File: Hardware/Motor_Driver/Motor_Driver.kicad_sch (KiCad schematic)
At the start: 2 parts, among them U1 IR4301, U2 LM4766

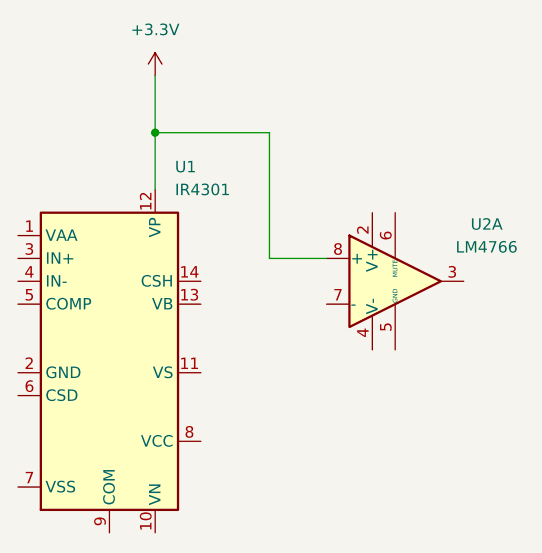
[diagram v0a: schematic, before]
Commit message: endret på shcemtatic, fjernet opamp
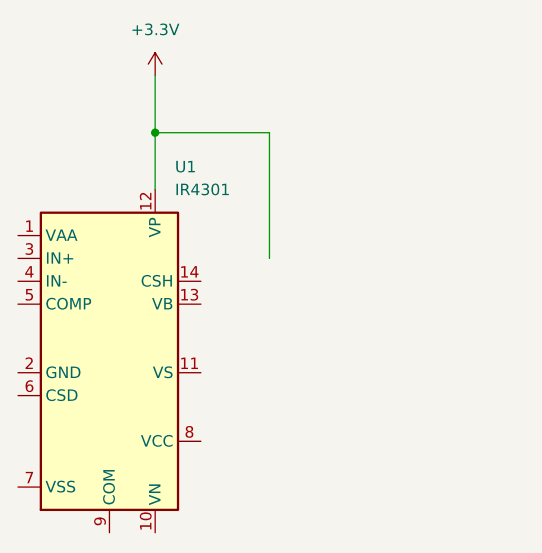
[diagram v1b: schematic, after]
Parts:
- removed U2: LM4766, Package_TO_SOT_THT:TO-220-15_P2.54x2.54mm_StaggerOdd_Lead4.58mm_Vertical, symbol Amplifier_Audio:LM4766
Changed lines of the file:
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@@
-		)
-	)
-	(wire
-		(pts
-			(xy 154.94 73.66) (xy 148.59 73.66)
-		)
-		(stroke
-			(width 0)
-			(type default)
-		)
-	)
-	(symbol
-		(lib_id "Amplifier_Audio:LM4766")
-		(at 162.56 76.2 0)
-		(unit 1)
-		(exclude_from_sim no)
-		(in_bom yes)
-		(on_board yes)
-		(dnp no)
-		(fields_autoplaced yes)
-		(property "Reference" "U2"
-			(at 172.72 69.8814 0)
-			(effects
-				(font
-					(size 1.27 1.27)
-				)
-			)
-		)
-		(property "Value" "LM4766"
-			(at 172.72 72.4214 0)
-			(effects
-				(font
-					(size 1.27 1.27)
-				)
-			)
-		)
-		(property "Footprint" "Package_TO_SOT_THT:TO-220-15_P2.54x2.54mm_StaggerOdd_Lead4.58mm_Vertical"
-			(at 162.56 76.2 0)
-			(effects
-				(font
-					(size 1.27 1.27)
-					(italic yes)
-				)
-				(hide yes)
-			)
-		)
-		(property "Datasheet" "http://www.ti.com/lit/ds/symlink/lm4766.pdf"
-			(at 162.56 76.2 0)
-			(effects
-				(font
-					(size 1.27 1.27)
-				)
-				(hide yes)
-			)
-		)
-		(property "Description" "Overture Audio Power Amplifier Series Dual 40W Audio Power Amplifier with Mute, TO-220-15"
-			(at 162.56 76.2 0)
-			(effects
-				(font
-					(size 1.27 1.27)
-				)
-				(hide yes)
-			)
-		)
-		(pin "3"
-		)
-		(pin "13"
-		)
-		(pin "15"
-		)
-		(pin "2"
-		)
-		(pin "5"
-		)
-		(pin "11"
-		)
-		(pin "9"
-		)
-		(pin "1"
-		)
-		(pin "14"
-		)
-		(pin "10"
-		)
-		(pin "6"
-		)
-		(pin "7"
-		)
-		(pin "4"
-		)
-		(pin "8"
-		)
-		(pin "12"
-		)
-		(instances
-			(project ""
-				(path "/ef03e5fb-dcf6-48d2-925e-8f1f54ddcbda"
-					(reference "U2")
-					(unit 1)
-				)
-			)
 		)
 	)
@@
 		)
 		(instances
-			(project ""
+			(project "Motor_Driver"
 				(path "/ef03e5fb-dcf6-48d2-925e-8f1f54ddcbda"
 					(reference "#PWR01")
@@
 		)
 		(instances
-			(project ""
+			(project "Motor_Driver"
 				(path "/ef03e5fb-dcf6-48d2-925e-8f1f54ddcbda"
 					(reference "U1")

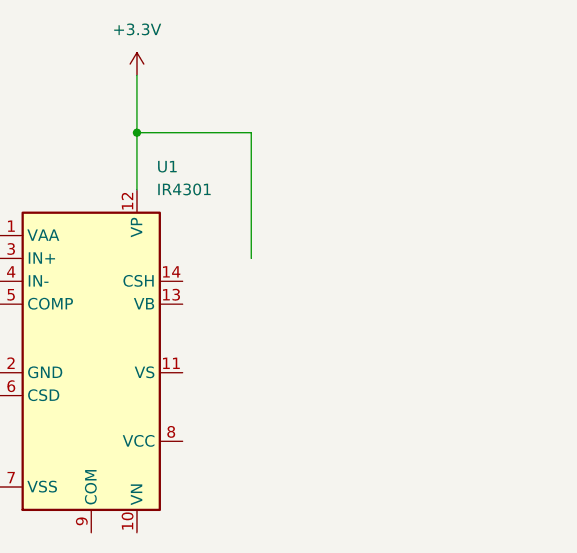
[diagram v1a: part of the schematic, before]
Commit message: La til en AND gate
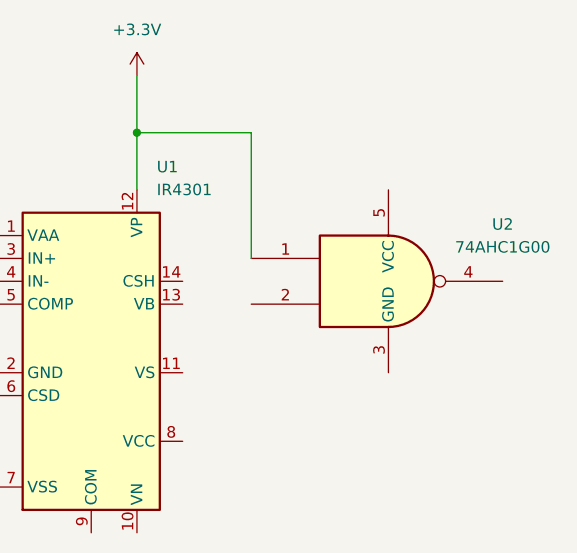
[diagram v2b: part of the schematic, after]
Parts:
- added U2: 74AHC1G00, symbol 74xGxx:74AHC1G00
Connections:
- net +3.3V: now also U2.1
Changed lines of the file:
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@@
+	)
+	(symbol
+		(lib_id "74xGxx:74AHC1G00")
+		(at 163.83 76.2 0)
+		(unit 1)
+		(exclude_from_sim no)
+		(in_bom yes)
+		(on_board yes)
+		(dnp no)
+		(fields_autoplaced yes)
+		(property "Reference" "U2"
+			(at 176.53 69.8814 0)
+			(effects
+				(font
+					(size 1.27 1.27)
+				)
+			)
+		)
+		(property "Value" "74AHC1G00"
+			(at 176.53 72.4214 0)
+			(effects
+				(font
+					(size 1.27 1.27)
+				)
+			)
+		)
+		(property "Footprint" ""
+			(at 163.83 76.2 0)
+			(effects
+				(font
+					(size 1.27 1.27)
+				)
+				(hide yes)
+			)
+		)
+		(property "Datasheet" "http://www.ti.com/lit/sg/scyt129e/scyt129e.pdf"
+			(at 163.83 76.2 0)
+			(effects
+				(font
+					(size 1.27 1.27)
+				)
+				(hide yes)
+			)
+		)
+		(property "Description" "Single NAND Gate, Low-Voltage CMOS"
+			(at 163.83 76.2 0)
+			(effects
+				(font
+					(size 1.27 1.27)
+				)
+				(hide yes)
+			)
+		)
+		(pin "4"
+		)
+		(pin "5"
+		)
+		(pin "2"
+		)
+		(pin "3"
+		)
+		(pin "1"
+		)
+		(instances
+			(project ""
+				(path "/ef03e5fb-dcf6-48d2-925e-8f1f54ddcbda"
+					(reference "U2")
+					(unit 1)
+				)
+			)
+		)
 	)
 	(symbol

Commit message: Lagt inn 2 USB-C porter
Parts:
- removed U1: IR4301, Package_DFN_QFN:Infineon_PQFN-22-15-4EP_6x5mm_P0.65mm, symbol Amplifier_Audio:IR4301
- removed U2: 74AHC1G00, symbol 74xGxx:74AHC1G00
- added P1, P2: USB_C_Plug, symbol Connector:USB_C_Plug
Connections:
- new net: P1.A1 (GND), P1.A12 (GND), P1.B1 (GND), P1.B12 (GND)
- new net: P1.A4 (VBUS), P1.A9 (VBUS), P1.B4 (VBUS), P1.B9 (VBUS)
- new net: P2.A1 (GND), P2.A12 (GND), P2.B1 (GND), P2.B12 (GND)
- new net: P2.A4 (VBUS), P2.A9 (VBUS), P2.B4 (VBUS), P2.B9 (VBUS)
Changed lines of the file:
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@@
 (kicad_sch
-	(version 20231120)
+	(version 20250114)
 	(generator "eeschema")
-	(generator_version "8.0")
+	(generator_version "9.0")
 	(paper "A4")
-	(junction
-		(at 135.89 59.69)
-		(diameter 0)
-		(color 0 0 0 0)
-	)
-	(wire
-		(pts
-			(xy 148.59 59.69) (xy 135.89 59.69)
-		)
-		(stroke
-			(width 0)
-			(type default)
-		)
-	)
-	(wire
-		(pts
-			(xy 135.89 59.69) (xy 135.89 66.04)
-		)
-		(stroke
-			(width 0)
-			(type default)
-		)
-	)
-	(wire
-		(pts
-			(xy 148.59 73.66) (xy 148.59 59.69)
-		)
-		(stroke
-			(width 0)
-			(type default)
-		)
-	)
-	(wire
-		(pts
-			(xy 135.89 53.34) (xy 135.89 59.69)
-		)
-		(stroke
-			(width 0)
-			(type default)
-		)
-	)
 	(symbol
-		(lib_id "power:+3.3V")
-		(at 135.89 53.34 0)
+		(lib_id "Connector:USB_C_Plug")
+		(at 30.48 53.34 0)
 		(unit 1)
 		(exclude_from_sim no)
@@
 		(dnp no)
 		(fields_autoplaced yes)
-		(property "Reference" "#PWR01"
-			(at 135.89 57.15 0)
-			(effects
-				(font
-					(size 1.27 1.27)
-				)
-				(hide yes)
-			)
-		)
-		(property "Value" "+3.3V"
-			(at 135.89 48.26 0)
+		(property "Reference" "P1"
+			(at 30.48 20.32 0)
+			(effects
+				(font
+					(size 1.27 1.27)
+				)
+			)
+		)
+		(property "Value" "USB_C_Plug"
+			(at 30.48 22.86 0)
 			(effects
 				(font
@@
 		)
 		(property "Footprint" ""
-			(at 135.89 53.34 0)
-			(effects
-				(font
-					(size 1.27 1.27)
-				)
-				(hide yes)
-			)
-		)
-		(property "Datasheet" ""
-			(at 135.89 53.34 0)
-			(effects
-				(font
-					(size 1.27 1.27)
-				)
-				(hide yes)
-			)
-		)
-		(property "Description" "Power symbol creates a global label with name \"+3.3V\""
-			(at 135.89 53.34 0)
-			(effects
-				(font
-					(size 1.27 1.27)
-				)
-				(hide yes)
-			)
-		)
-		(pin "1"
+			(at 34.29 53.34 0)
+			(effects
+				(font
+					(size 1.27 1.27)
+				)
+				(hide yes)
+			)
+		)
+		(property "Datasheet" "https://www.usb.org/sites/default/files/documents/usb_type-c.zip"
+			(at 34.29 53.34 0)
+			(effects
+				(font
+					(size 1.27 1.27)
+				)
+				(hide yes)
+			)
+		)
+		(property "Description" "USB Type-C Plug connector"
+			(at 30.48 53.34 0)
+			(effects
+				(font
+					(size 1.27 1.27)
+				)
+				(hide yes)
+			)
+		)
+		(pin "A1"
+		)
+		(pin "S1"
+		)
+		(pin "A12"
+		)
+		(pin "B9"
+		)
+		(pin "B1"
+		)
+		(pin "B12"
+		)
+		(pin "B4"
+		)
+		(pin "A4"
+		)
+		(pin "A9"
+		)
+		(pin "A5"
+		)
+		(pin "A6"
+		)
+		(pin "B10"
+		)
+		(pin "B11"
+		)
+		(pin "A3"
+		)
+		(pin "A7"
+		)
+		(pin "A2"
+		)
+		(pin "B3"
+		)
+		(pin "B2"
+		)
+		(pin "A10"
+		)
+		(pin "A11"
+		)
+		(pin "B5"
+		)
+		(pin "A8"
+		)
+		(pin "B8"
 		)
 		(instances
-			(project "Motor_Driver"
+			(project ""
 				(path "/ef03e5fb-dcf6-48d2-925e-8f1f54ddcbda"
-					(reference "#PWR01")
+					(reference "P1")
 					(unit 1)
 				)
@@
 	)
 	(symbol
-		(lib_id "74xGxx:74AHC1G00")
-		(at 163.83 76.2 0)
+		(lib_id "Connector:USB_C_Plug")
+		(at 30.48 135.89 0)
 		(unit 1)
 		(exclude_from_sim no)
@@
 		(dnp no)
 		(fields_autoplaced yes)
-		(property "Reference" "U2"
-			(at 176.53 69.8814 0)
-			(effects
-				(font
-					(size 1.27 1.27)
-				)
-			)
-		)
-		(property "Value" "74AHC1G00"
-			(at 176.53 72.4214 0)
+		(property "Reference" "P2"
+			(at 30.48 102.87 0)
+			(effects
+				(font
+					(size 1.27 1.27)
+				)
+			)
+		)
+		(property "Value" "USB_C_Plug"
+			(at 30.48 105.41 0)
 			(effects
 				(font
@@
 		)
 		(property "Footprint" ""
-			(at 163.83 76.2 0)
-			(effects
-				(font
-					(size 1.27 1.27)
-				)
-				(hide yes)
-			)
-		)
-		(property "Datasheet" "http://www.ti.com/lit/sg/scyt129e/scyt129e.pdf"
-			(at 163.83 76.2 0)
-			(effects
-				(font
-					(size 1.27 1.27)
-				)
-				(hide yes)
-			)
-		)
-		(property "Description" "Single NAND Gate, Low-Voltage CMOS"
-			(at 163.83 76.2 0)
-			(effects
-				(font
-					(size 1.27 1.27)
-				)
-				(hide yes)
-			)
-		)
-		(pin "4"
-		)
-		(pin "5"
-		)
-		(pin "2"
-		)
-		(pin "3"
-		)
-		(pin "1"
-		)
-		(instances
-			(project ""
-				(path "/ef03e5fb-dcf6-48d2-925e-8f1f54ddcbda"
-					(reference "U2")
-					(unit 1)
-				)
-			)
-		)
-	)
-	(symbol
-		(lib_id "Amplifier_Audio:IR4301")
-		(at 130.81 86.36 0)
-		(unit 1)
-		(exclude_from_sim no)
-		(in_bom yes)
-		(on_board yes)
-		(dnp no)
-		(fields_autoplaced yes)
-		(property "Reference" "U1"
-			(at 138.0841 63.5 0)
-			(effects
-				(font
-					(size 1.27 1.27)
-				)
-				(justify left)
-			)
-		)
-		(property "Value" "IR4301"
-			(at 138.0841 66.04 0)
-			(effects
-				(font
-					(size 1.27 1.27)
-				)
-				(justify left)
-			)
-		)
-		(property "Footprint" "Package_DFN_QFN:Infineon_PQFN-22-15-4EP_6x5mm_P0.65mm"
-			(at 130.81 86.36 0)
-			(effects
-				(font
-					(size 1.27 1.27)
-					(italic yes)
-				)
-				(hide yes)
-			)
-		)
-		(property "Datasheet" "https://www.infineon.com/dgdl/ir4301.pdf?fileId=5546d462533600a4015355d5fc691819"
-			(at 130.81 86.36 0)
-			(effects
-				(font
-					(size 1.27 1.27)
-				)
-				(hide yes)
-			)
-		)
-		(property "Description" "PowIRaudio Integrated Analog Input Class D Audio Amplifier, 160W/4ohm, 80V, PQFN-22"
-			(at 130.81 86.36 0)
-			(effects
-				(font
-					(size 1.27 1.27)
-				)
-				(hide yes)
-			)
-		)
-		(pin "1"
-		)
-		(pin "11"
-		)
-		(pin "13"
-		)
-		(pin "14"
-		)
-		(pin "15"
-		)
-		(pin "2"
-		)
-		(pin "3"
-		)
-		(pin "4"
-		)
-		(pin "6"
-		)
-		(pin "12"
-		)
-		(pin "10"
-		)
-		(pin "7"
-		)
-		(pin "8"
-		)
-		(pin "5"
-		)
-		(pin "9"
+			(at 34.29 135.89 0)
+			(effects
+				(font
+					(size 1.27 1.27)
+				)
+				(hide yes)
+			)
+		)
+		(property "Datasheet" "https://www.usb.org/sites/default/files/documents/usb_type-c.zip"
+			(at 34.29 135.89 0)
+			(effects
+				(font
+					(size 1.27 1.27)
+				)
+				(hide yes)
+			)
+		)
+		(property "Description" "USB Type-C Plug connector"
+			(at 30.48 135.89 0)
+			(effects
+				(font
+					(size 1.27 1.27)
+				)
+				(hide yes)
+			)
+		)
+		(pin "A1"
+		)
+		(pin "S1"
+		)
+		(pin "A12"
+		)
+		(pin "B9"
+		)
+		(pin "B1"
+		)
+		(pin "B12"
+		)
+		(pin "B4"
+		)
+		(pin "A4"
+		)
+		(pin "A9"
+		)
+		(pin "A5"
+		)
+		(pin "A6"
+		)
+		(pin "B10"
+		)
+		(pin "B11"
+		)
+		(pin "A3"
+		)
+		(pin "A7"
+		)
+		(pin "A2"
+		)
+		(pin "B3"
+		)
+		(pin "B2"
+		)
+		(pin "A10"
+		)
+		(pin "A11"
+		)
+		(pin "B5"
+		)
+		(pin "A8"
+		)
+		(pin "B8"
 		)
 		(instances
 			(project "Motor_Driver"
 				(path "/ef03e5fb-dcf6-48d2-925e-8f1f54ddcbda"
-					(reference "U1")
+					(reference "P2")
 					(unit 1)
 				)
@@
 		)
 	)
+	(embedded_fonts no)
 )

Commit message: la til en melding i schematicehn
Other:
- note added: "Dette er en test av githubby"
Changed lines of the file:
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@@
 	(generator_version "9.0")
 	(paper "A4")
+	(text "Dette er en test av githubby\n"
+		(exclude_from_sim no)
+		(at 155.702 95.25 0)
+		(effects
+			(font
+				(size 5.08 5.08)
+			)
+		)
+	)
 	(symbol
 		(lib_id "Connector:USB_C_Plug")
